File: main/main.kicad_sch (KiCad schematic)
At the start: 3 parts, among them SW1 SW_DPST_x2

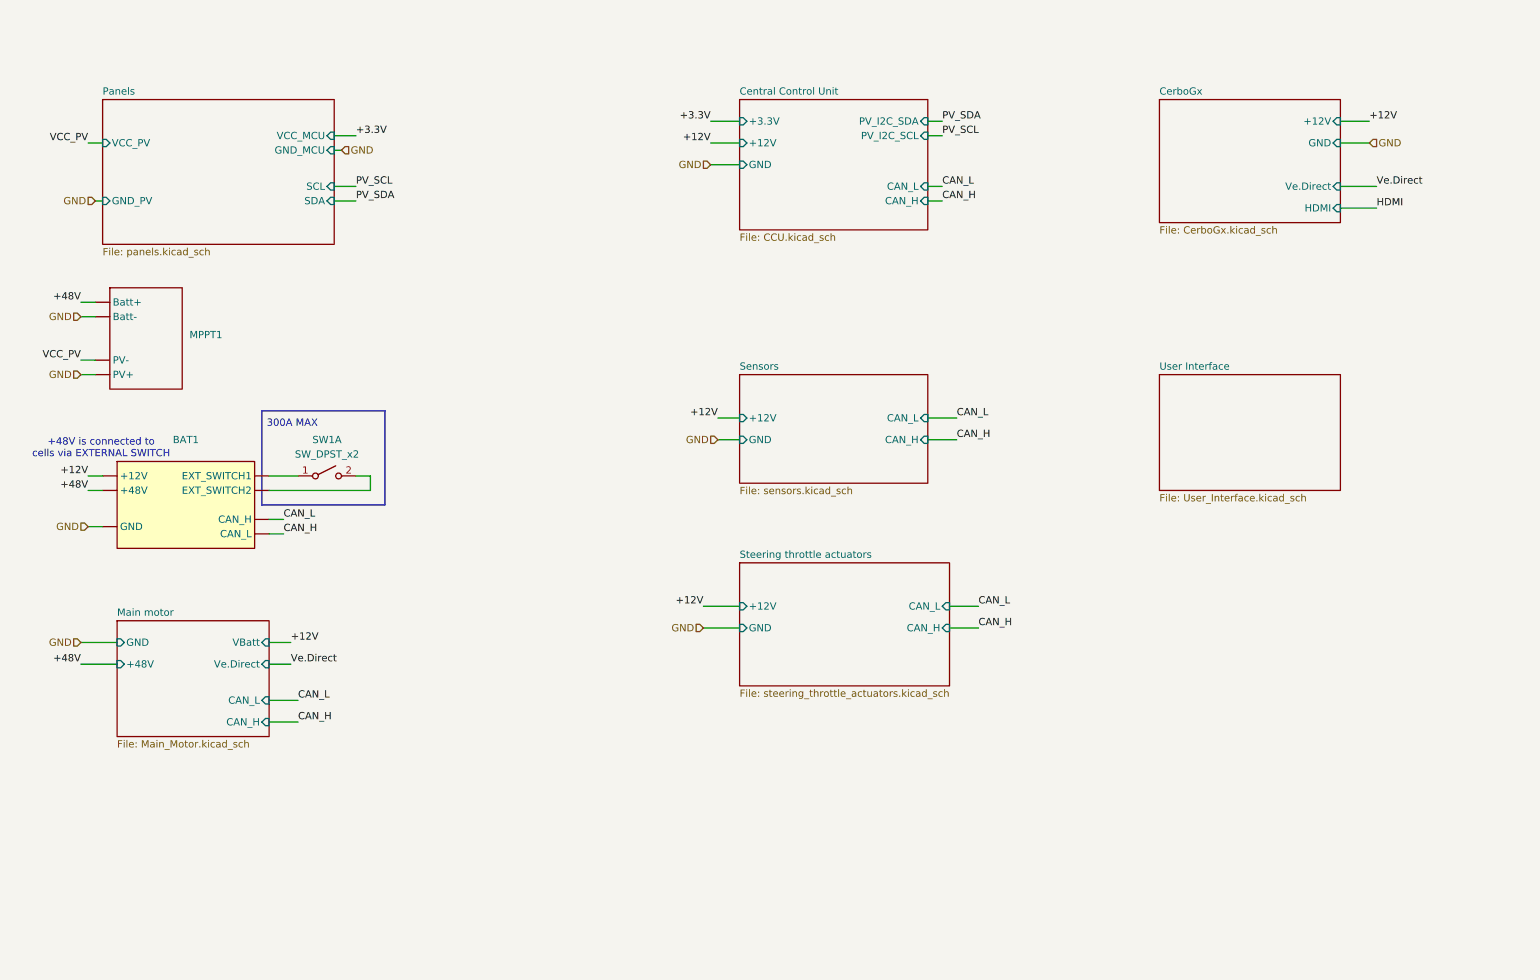
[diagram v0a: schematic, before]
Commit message: added UI, +12/gnd to 4 pin adapter symbol, added NMEA2000 gateway symbol
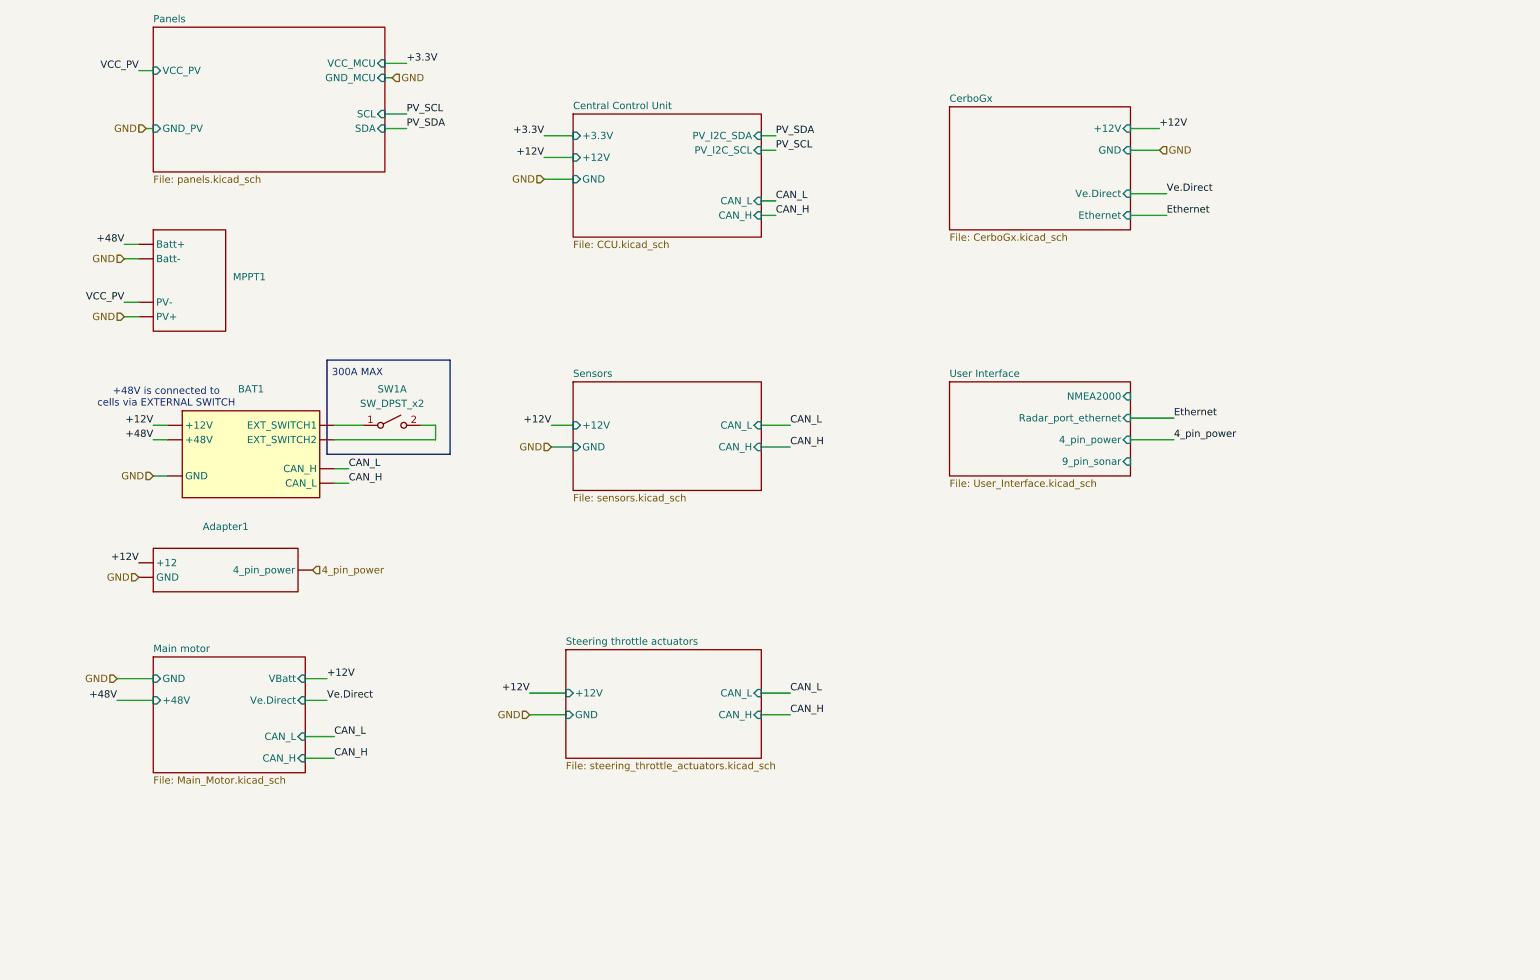
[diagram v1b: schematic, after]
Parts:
- added Adapter1: ~, symbol New_Library_0:+12/gnd_to_4_pin_adapter
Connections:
- net +12V: now also Adapter1. (GND)
- net GND: now also Adapter1. (GND)
- new net 4_pin_power: Adapter1. (GND)
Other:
- sheet CerboGx ports: added Ethernet; removed HDMI
- sheet User Interface ports: added 4_pin_power, 9_pin_sonar, NMEA2000, Radar_port_ethernet; removed none
- moved on the sheet: BAT1, MPPT1, SW1A

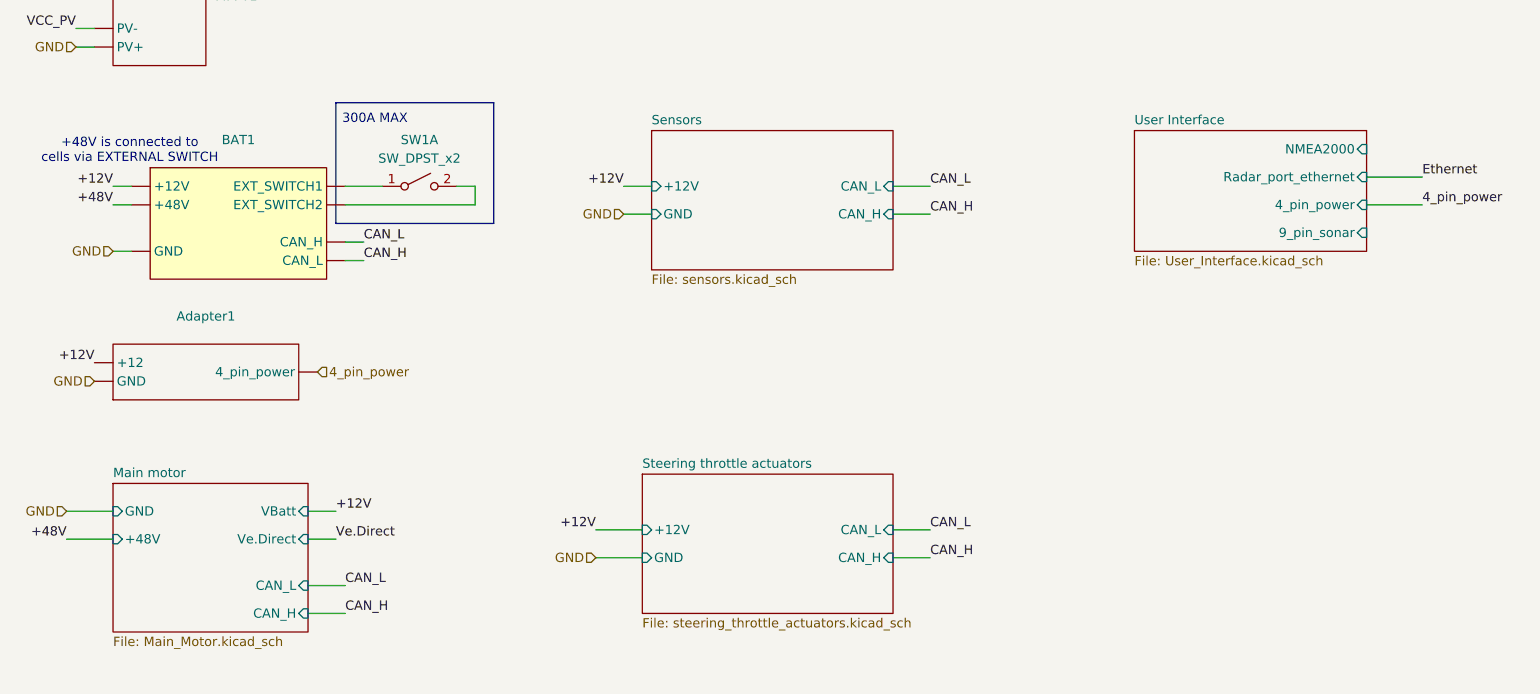
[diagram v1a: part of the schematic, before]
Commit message: added new output from main motor and connected it to NMEA input in monitor
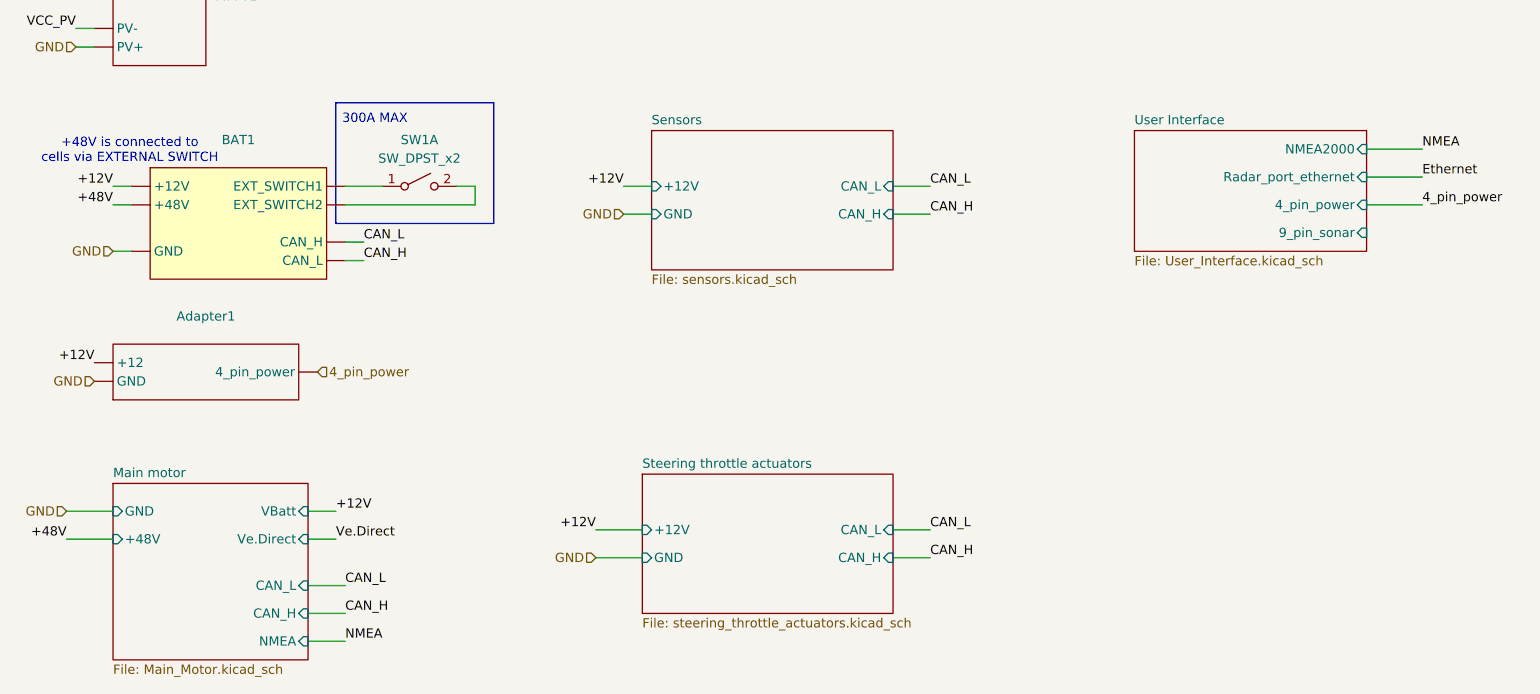
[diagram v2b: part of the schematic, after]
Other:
- sheet Main motor ports: added NMEA; removed none
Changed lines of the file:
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@@
+	(wire
+		(pts
+			(xy 207.01 86.36) (xy 214.63 86.36)
+		)
+		(stroke
+			(width 0)
+			(type default)
+		)
+	)
 	(wire
 		(pts
@@
 		(pts
 			(xy 101.6 142.24) (xy 107.95 142.24)
+		)
+		(stroke
+			(width 0)
+			(type default)
+		)
+	)
+	(wire
+		(pts
+			(xy 62.23 153.67) (xy 67.31 153.67)
 		)
 		(stroke
@@
 		)
 	)
+	(label "NMEA"
+		(at 67.31 153.67 0)
+		(fields_autoplaced yes)
+		(effects
+			(font
+				(size 1.27 1.27)
+			)
+			(justify left bottom)
+		)
+	)
 	(label "+12V"
 		(at 212.09 39.37 0)
@@
 	(label "CAN_L"
 		(at 144.78 52.07 0)
+		(fields_autoplaced yes)
+		(effects
+			(font
+				(size 1.27 1.27)
+			)
+			(justify left bottom)
+		)
+	)
+	(label "NMEA"
+		(at 214.63 86.36 0)
 		(fields_autoplaced yes)
 		(effects
@@
 	(sheet
 		(at 35.56 132.08)
-		(size 26.67 20.32)
+		(size 26.67 24.13)
 		(fields_autoplaced yes)
 		(stroke
@@
 		)
 		(property "Sheetfile" "Main_Motor.kicad_sch"
-			(at 35.56 152.9846 0)
+			(at 35.56 156.7946 0)
 			(effects
 				(font
@@
 			(effects
 				(font
+					(size 1.27 1.27)
+				)
+				(justify right)
+			)
+		)
+		(pin "NMEA" input
+			(at 62.23 153.67 0)
+			(effects
+				(font

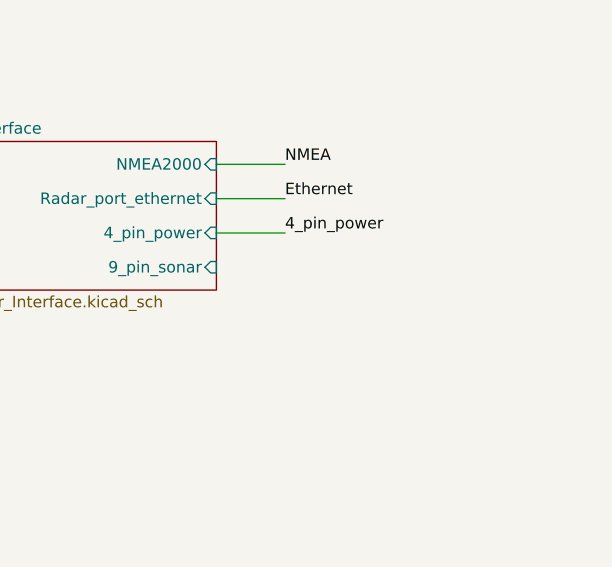
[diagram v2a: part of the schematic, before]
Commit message: added sonar
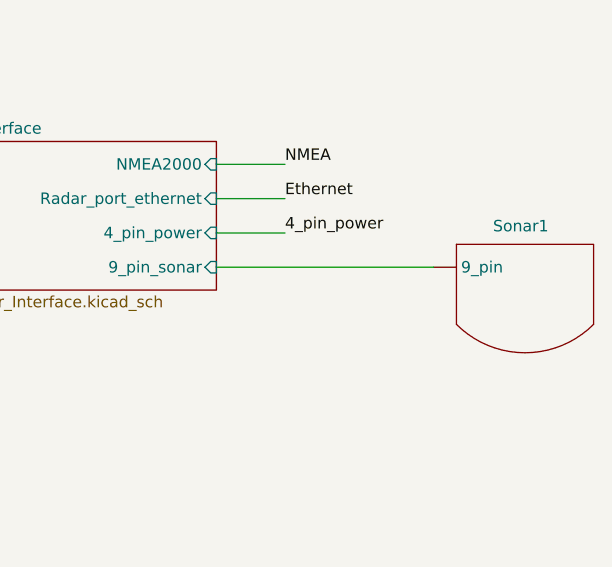
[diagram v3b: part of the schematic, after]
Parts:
- added Sonar1: ~, symbol New_Library_0:Sonar
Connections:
- net User Interface/9_pin_sonar: now also Sonar1. (9_pin)
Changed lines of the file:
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@@
+	(wire
+		(pts
+			(xy 207.01 97.79) (xy 231.14 97.79)
+		)
+		(stroke
+			(width 0)
+			(type default)
+		)
+	)
 	(wire
 		(pts
@@
 					(unit 1)
 				)
+			)
+		)
+	)
+	(symbol
+		(lib_id "New_Library_0:Sonar")
+		(at 241.3 100.33 0)
+		(unit 1)
+		(exclude_from_sim no)
+		(in_bom yes)
+		(on_board yes)
+		(dnp no)
+		(property "Reference" "Sonar1"
+			(at 237.744 93.218 0)
+			(effects
+				(font
+					(size 1.27 1.27)
+				)
+				(justify left)
+			)
+		)
+		(property "Value" "~"
+			(at 250.19 102.5431 0)
+			(effects
+				(font
+					(size 1.27 1.27)
+				)
+				(justify left)
+			)
+		)
+		(property "Footprint" ""
+			(at 241.3 100.33 0)
+			(effects
+				(font
+					(size 1.27 1.27)
+				)
+				(hide yes)
+			)
+		)
+		(property "Datasheet" ""
+			(at 241.3 100.33 0)
+			(effects
+				(font
+					(size 1.27 1.27)
+				)
+				(hide yes)
+			)
+		)
+		(property "Description" ""
+			(at 241.3 100.33 0)
+			(effects
+				(font
+					(size 1.27 1.27)
+				)
+				(hide yes)
+			)
+		)
+		(pin ""
+		)
+		(instances
+			(project ""
+				(path "/54fbbba9-a737-4199-9a4b-f9fa49b3de5e"
+					(reference "Sonar1")
+					(unit 1)
+				)

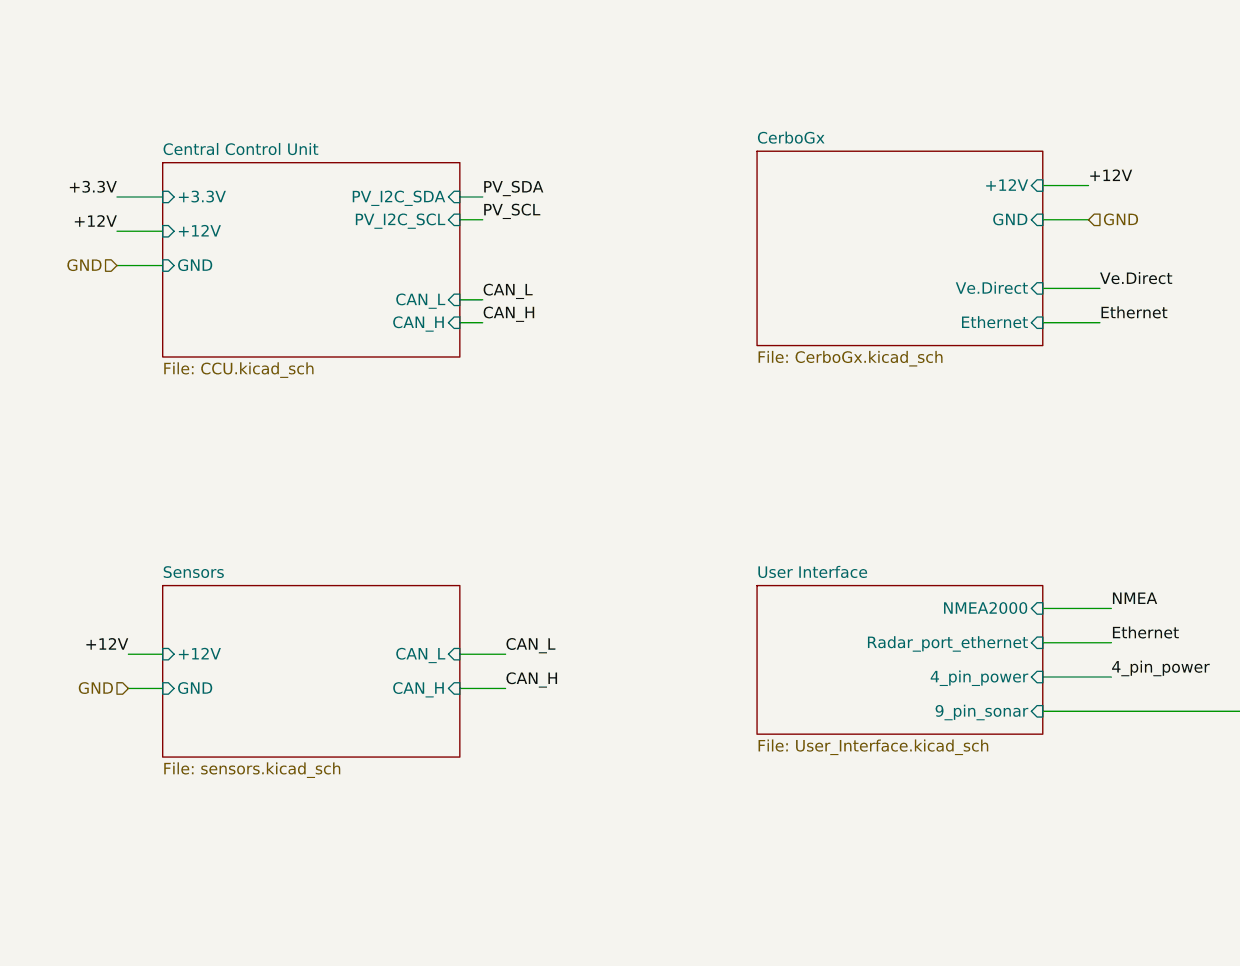
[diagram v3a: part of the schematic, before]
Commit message: Added AMS, LEDs
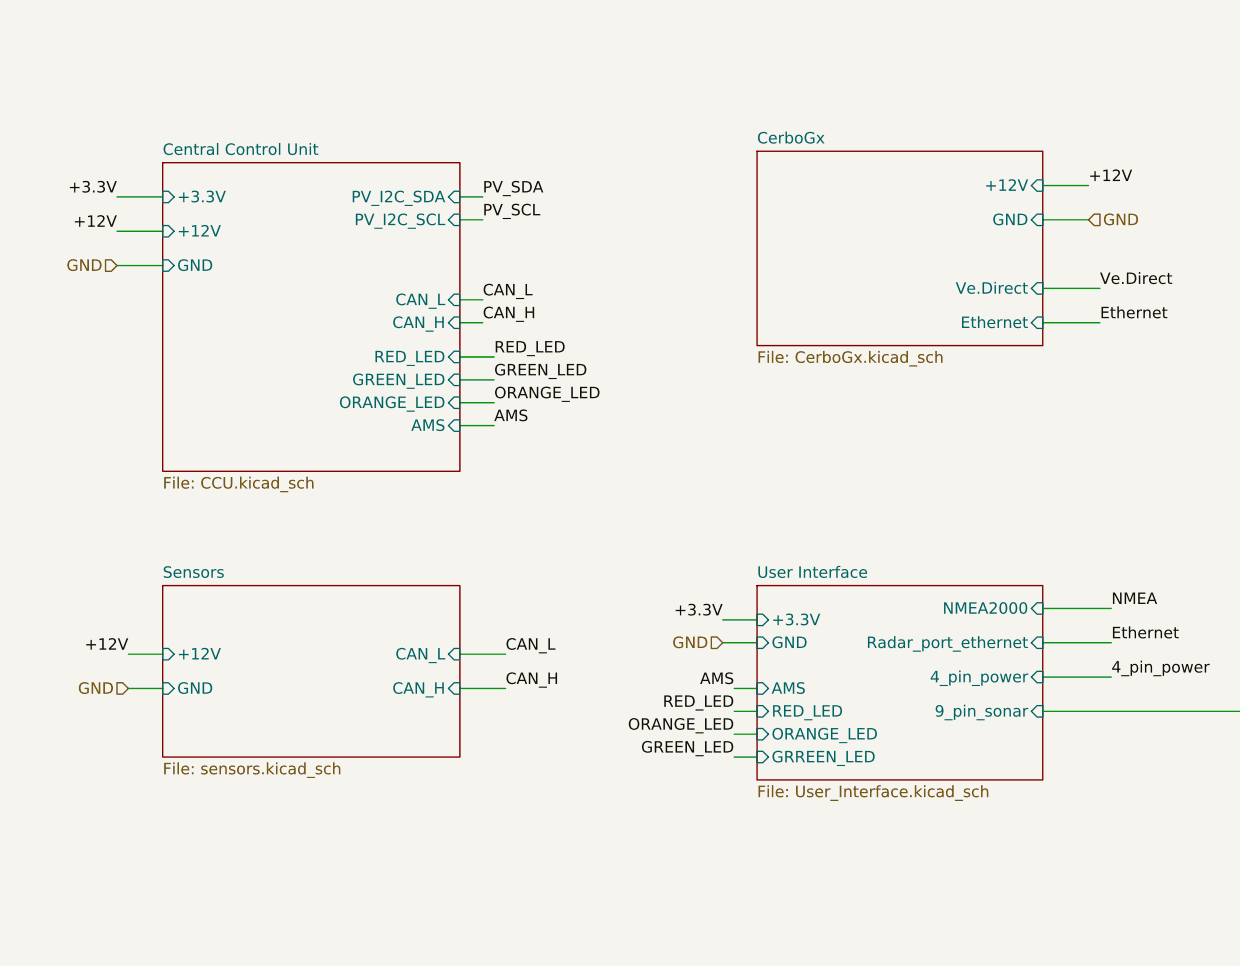
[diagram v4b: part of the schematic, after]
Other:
- sheet Central Control Unit ports: added AMS, GREEN_LED, ORANGE_LED, RED_LED; removed none
- sheet User Interface ports: added +3.3V, AMS, GND, GRREEN_LED, ORANGE_LED, RED_LED; removed none
